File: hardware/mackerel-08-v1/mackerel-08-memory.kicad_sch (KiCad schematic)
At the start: 8 parts, among them U10 AS6C4008-55PCN, U11 AS6C4008-55PCN, U12 AS6C4008-55PCN, U13 SST39SF040, U6 AS6C4008-55PCN, U7 AS6C4008-55PCN, U8 AS6C4008-55PCN, U9 AS6C4008-55PCN

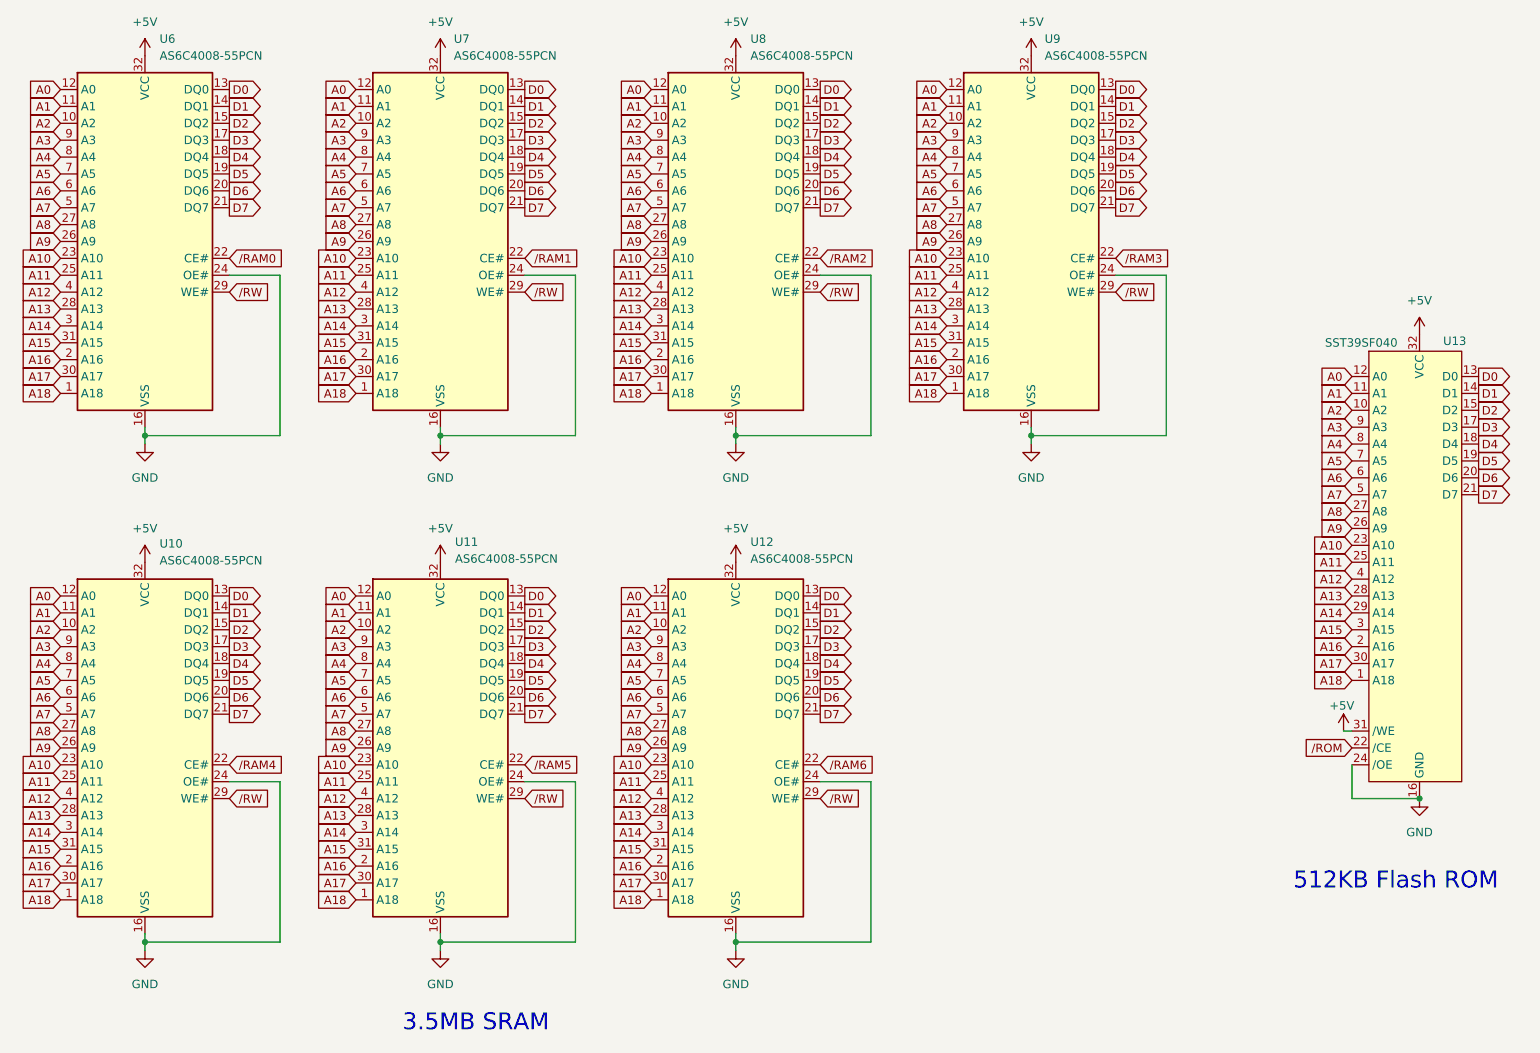
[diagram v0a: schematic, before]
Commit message: Mack-08 1.1 schematic fixes done, needs final routing
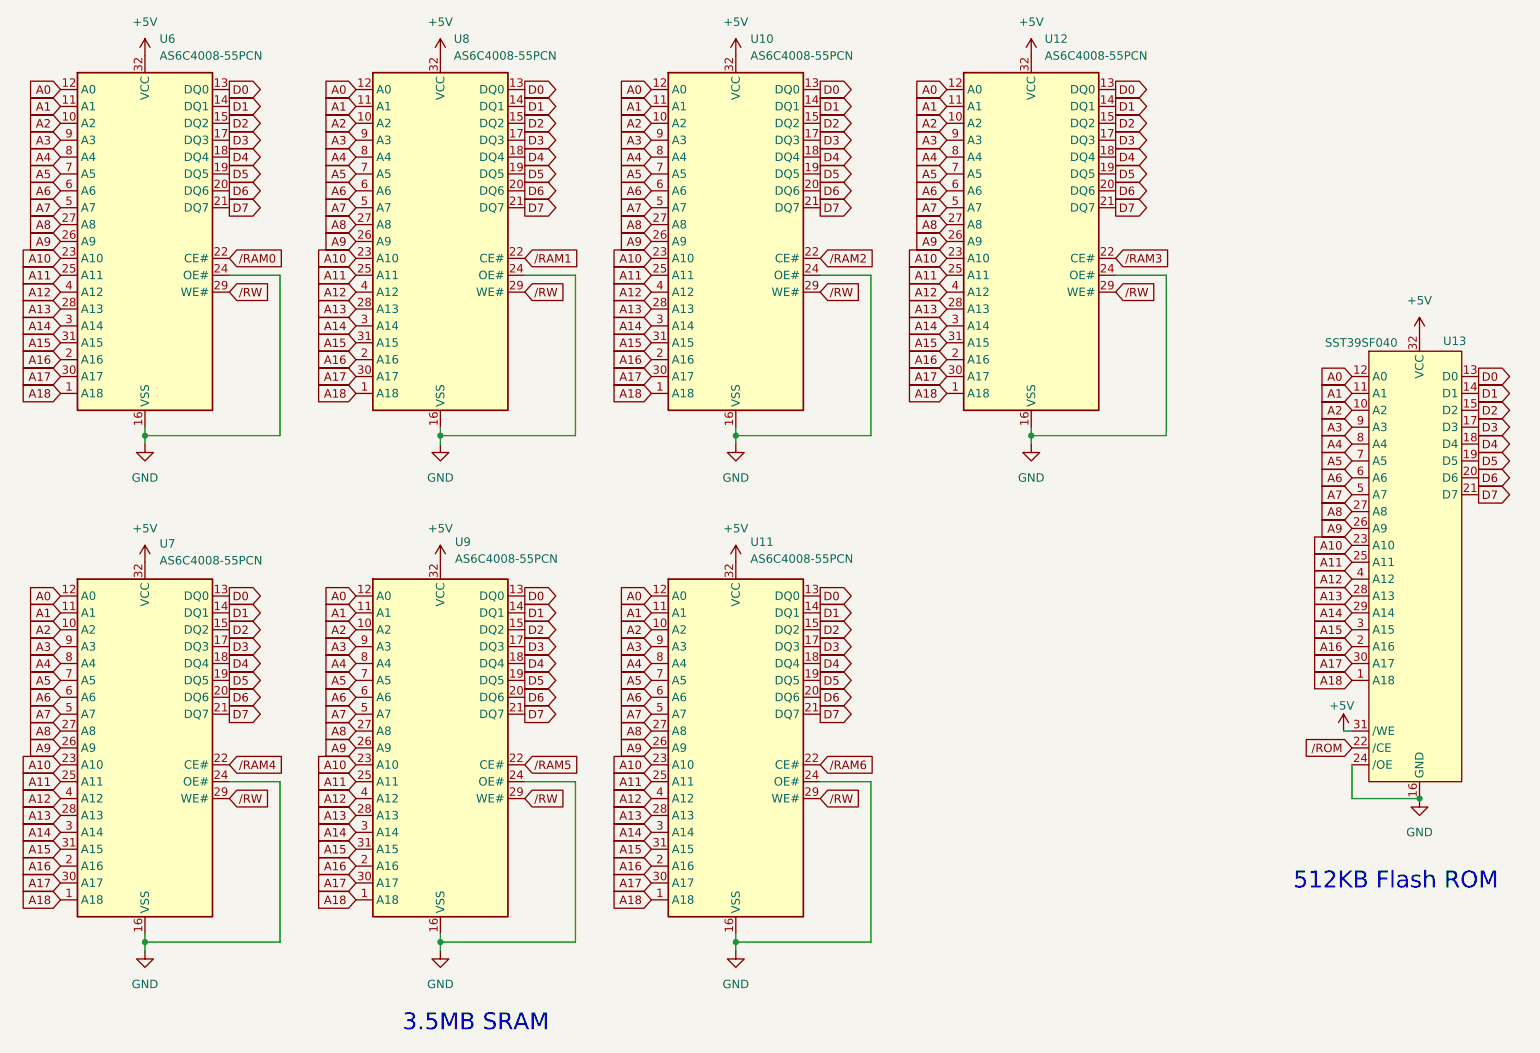
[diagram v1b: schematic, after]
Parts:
- renumbered U8 to U10, U12 to U11, U9 to U12, U10 to U7, U7 to U8, U11 to U9
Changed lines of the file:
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@@
 		(dnp no)
 		(fields_autoplaced yes)
-		(property "Reference" "#PWR024"
+		(property "Reference" "#PWR027"
 			(at 133.35 104.14 0)
 			(effects
@@
 			(project "mackerel-08-v1"
 				(path "/d8b1bce0-db11-4fa6-8e54-fcae9a8fcfc2/5f34c349-ebaa-45fd-b23a-8893b29db344"
-					(reference "#PWR024")
+					(reference "#PWR027")
 					(unit 1)
 				)
@@
 		(dnp no)
 		(fields_autoplaced yes)
-		(property "Reference" "#PWR034"
+		(property "Reference" "#PWR025"
 			(at 133.35 27.94 0)
 			(effects
@@
 			(project "mackerel-08-v1"
 				(path "/d8b1bce0-db11-4fa6-8e54-fcae9a8fcfc2/5f34c349-ebaa-45fd-b23a-8893b29db344"
-					(reference "#PWR034")
+					(reference "#PWR025")
 					(unit 1)
 				)
@@
 		(dnp no)
 		(fields_autoplaced yes)
-		(property "Reference" "#PWR023"
+		(property "Reference" "#PWR032"
 			(at 236.22 69.85 0)
 			(effects
@@
 			(project "mackerel-08-v1"
 				(path "/d8b1bce0-db11-4fa6-8e54-fcae9a8fcfc2/5f34c349-ebaa-45fd-b23a-8893b29db344"
-					(reference "#PWR023")
+					(reference "#PWR032")
 					(unit 1)
 				)
@@
 		(dnp no)
 		(fields_autoplaced yes)
-		(property "Reference" "U8"
+		(property "Reference" "U10"
 			(at 135.5441 21.59 0)
 			(effects
@@
 			(project "mackerel-08-v1"
 				(path "/d8b1bce0-db11-4fa6-8e54-fcae9a8fcfc2/5f34c349-ebaa-45fd-b23a-8893b29db344"
-					(reference "U8")
+					(reference "U10")
 					(unit 1)
 				)
@@
 		(dnp no)
 		(fields_autoplaced yes)
-		(property "Reference" "#PWR025"
+		(property "Reference" "#PWR021"
 			(at 88.9 27.94 0)
 			(effects
@@
 			(project "mackerel-08-v1"
 				(path "/d8b1bce0-db11-4fa6-8e54-fcae9a8fcfc2/5f34c349-ebaa-45fd-b23a-8893b29db344"
-					(reference "#PWR025")
+					(reference "#PWR021")
 					(unit 1)
 				)
@@
 		(dnp no)
 		(fields_autoplaced yes)
-		(property "Reference" "U7"
+		(property "Reference" "U8"
 			(at 90.9194 21.59 0)
 			(effects
@@
 			(project "mackerel-08-v1"
 				(path "/d8b1bce0-db11-4fa6-8e54-fcae9a8fcfc2/5f34c349-ebaa-45fd-b23a-8893b29db344"
-					(reference "U7")
+					(reference "U8")
 					(unit 1)
 				)
@@
 		(on_board yes)
 		(dnp no)
-		(property "Reference" "#PWR028"
+		(property "Reference" "#PWR031"
 			(at 224.79 129.54 0)
 			(effects
@@
 			(project "mackerel-08-v1"
 				(path "/d8b1bce0-db11-4fa6-8e54-fcae9a8fcfc2/5f34c349-ebaa-45fd-b23a-8893b29db344"
-					(reference "#PWR028")
+					(reference "#PWR031")
 					(unit 1)
 				)
@@
 		(dnp no)
 		(fields_autoplaced yes)
-		(property "Reference" "#PWR039"
+		(property "Reference" "#PWR020"
 			(at 44.45 165.1 0)
 			(effects
@@
 			(project "mackerel-08-v1"
 				(path "/d8b1bce0-db11-4fa6-8e54-fcae9a8fcfc2/5f34c349-ebaa-45fd-b23a-8893b29db344"
-					(reference "#PWR039")
+					(reference "#PWR020")
 					(unit 1)
 				)
@@
 		(dnp no)
 		(fields_autoplaced yes)
-		(property "Reference" "#PWR029"
+		(property "Reference" "#PWR028"
 			(at 133.35 165.1 0)
 			(effects
@@
 			(project "mackerel-08-v1"
 				(path "/d8b1bce0-db11-4fa6-8e54-fcae9a8fcfc2/5f34c349-ebaa-45fd-b23a-8893b29db344"
-					(reference "#PWR029")
+					(reference "#PWR028")
 					(unit 1)
 				)
@@
 		(dnp no)
 		(fields_autoplaced yes)
-		(property "Reference" "#PWR035"
+		(property "Reference" "#PWR017"
 			(at 44.45 27.94 0)
 			(effects
@@
 			(project "mackerel-08-v1"
 				(path "/d8b1bce0-db11-4fa6-8e54-fcae9a8fcfc2/5f34c349-ebaa-45fd-b23a-8893b29db344"
-					(reference "#PWR035")
+					(reference "#PWR017")
 					(unit 1)
 				)
@@
 		(dnp no)
 		(fields_autoplaced yes)
-		(property "Reference" "#PWR036"
+		(property "Reference" "#PWR019"
 			(at 44.45 104.14 0)
 			(effects
@@
 			(project "mackerel-08-v1"
 				(path "/d8b1bce0-db11-4fa6-8e54-fcae9a8fcfc2/5f34c349-ebaa-45fd-b23a-8893b29db344"
-					(reference "#PWR036")
+					(reference "#PWR019")
 					(unit 1)
 				)
@@
 		(dnp no)
 		(fields_autoplaced yes)
-		(property "Reference" "U11"
+		(property "Reference" "U9"
 			(at 91.0941 97.282 0)
 			(effects
@@
 			(project "mackerel-08-v1"
 				(path "/d8b1bce0-db11-4fa6-8e54-fcae9a8fcfc2/5f34c349-ebaa-45fd-b23a-8893b29db344"
-					(reference "U11")
+					(reference "U9")
 					(unit 1)
 				)
@@
 		(dnp no)
 		(fields_autoplaced yes)
-		(property "Reference" "#PWR037"
+		(property "Reference" "#PWR026"
 			(at 133.35 88.9 0)
 			(effects
@@
 			(project "mackerel-08-v1"
 				(path "/d8b1bce0-db11-4fa6-8e54-fcae9a8fcfc2/5f34c349-ebaa-45fd-b23a-8893b29db344"
-					(reference "#PWR037")
+					(reference "#PWR026")
 					(unit 1)
 				)
@@
 		(dnp no)
 		(fields_autoplaced yes)
-		(property "Reference" "U10"
+		(property "Reference" "U7"
 			(at 46.6441 97.536 0)
 			(effects
@@
 			(project "mackerel-08-v1"
 				(path "/d8b1bce0-db11-4fa6-8e54-fcae9a8fcfc2/5f34c349-ebaa-45fd-b23a-8893b29db344"
-					(reference "U10")
+					(reference "U7")
 					(unit 1)
 				)
@@
 		(dnp no)
 		(fields_autoplaced yes)
-		(property "Reference" "U9"
+		(property "Reference" "U12"
 			(at 179.8194 21.59 0)
 			(effects
@@
 			(project "mackerel-08-v1"
 				(path "/d8b1bce0-db11-4fa6-8e54-fcae9a8fcfc2/5f34c349-ebaa-45fd-b23a-8893b29db344"
-					(reference "U9")
+					(reference "U12")
 					(unit 1)
 				)
@@
 		(dnp no)
 		(fields_autoplaced yes)
-		(property "Reference" "#PWR026"
+		(property "Reference" "#PWR023"
 			(at 88.9 104.14 0)
 			(effects
@@
 			(project "mackerel-08-v1"
 				(path "/d8b1bce0-db11-4fa6-8e54-fcae9a8fcfc2/5f34c349-ebaa-45fd-b23a-8893b29db344"
-					(reference "#PWR026")
+					(reference "#PWR023")
 					(unit 1)
 				)
@@
 		(dnp no)
 		(fields_autoplaced yes)
-		(property "Reference" "#PWR038"
+		(property "Reference" "#PWR018"
 			(at 44.45 88.9 0)
 			(effects
@@
 			(project "mackerel-08-v1"
 				(path "/d8b1bce0-db11-4fa6-8e54-fcae9a8fcfc2/5f34c349-ebaa-45fd-b23a-8893b29db344"
-					(reference "#PWR038")
+					(reference "#PWR018")
 					(unit 1)
 				)
@@
 		(dnp no)
 		(fields_autoplaced yes)
-		(property "Reference" "#PWR032"
+		(property "Reference" "#PWR030"
 			(at 177.8 88.9 0)
 			(effects
@@
 			(project "mackerel-08-v1"
 				(path "/d8b1bce0-db11-4fa6-8e54-fcae9a8fcfc2/5f34c349-ebaa-45fd-b23a-8893b29db344"
-					(reference "#PWR032")
+					(reference "#PWR030")
 					(unit 1)
 				)
@@
 		(dnp no)
 		(fields_autoplaced yes)
-		(property "Reference" "U12"
+		(property "Reference" "U11"
 			(at 135.5441 97.282 0)
 			(effects
@@
 			(project "mackerel-08-v1"
 				(path "/d8b1bce0-db11-4fa6-8e54-fcae9a8fcfc2/5f34c349-ebaa-45fd-b23a-8893b29db344"
-					(reference "U12")
+					(reference "U11")
 					(unit 1)
 				)
@@
 		(dnp no)
 		(fields_autoplaced yes)
-		(property "Reference" "#PWR030"
+		(property "Reference" "#PWR022"
 			(at 88.9 88.9 0)
 			(effects
@@
 			(project "mackerel-08-v1"
 				(path "/d8b1bce0-db11-4fa6-8e54-fcae9a8fcfc2/5f34c349-ebaa-45fd-b23a-8893b29db344"
-					(reference "#PWR030")
+					(reference "#PWR022")
 					(unit 1)
 				)
@@
 		(dnp no)
 		(fields_autoplaced yes)
-		(property "Reference" "#PWR031"
+		(property "Reference" "#PWR024"
 			(at 88.9 165.1 0)
 			(effects
@@
 			(project "mackerel-08-v1"
 				(path "/d8b1bce0-db11-4fa6-8e54-fcae9a8fcfc2/5f34c349-ebaa-45fd-b23a-8893b29db344"
-					(reference "#PWR031")
+					(reference "#PWR024")
 					(unit 1)
 				)
@@
 		(dnp no)
 		(fields_autoplaced yes)
-		(property "Reference" "#PWR027"
+		(property "Reference" "#PWR029"
 			(at 177.8 27.94 0)
 			(effects
@@
 			(project "mackerel-08-v1"
 				(path "/d8b1bce0-db11-4fa6-8e54-fcae9a8fcfc2/5f34c349-ebaa-45fd-b23a-8893b29db344"
-					(reference "#PWR027")
-					(unit 1)
-				)
+					(reference "#PWR029")
+					(unit 1)
+				)

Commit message: Add Mackerel-08 BOM list
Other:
- title: Mackerel-08 SBC v1 -> Mackerel-08 SBC v1.1
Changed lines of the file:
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@@
 	(paper "A")
 	(title_block
-		(title "Mackerel-08 SBC v1")
+		(title "Mackerel-08 SBC v1.1")
 		(date "2024-08-22")
 		(rev "1.1")
